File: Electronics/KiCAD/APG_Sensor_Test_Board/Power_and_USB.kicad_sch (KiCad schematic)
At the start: 10 parts, among them J4 USB_C_Receptacle_USB2.0_16P, U6 TLV1117-33

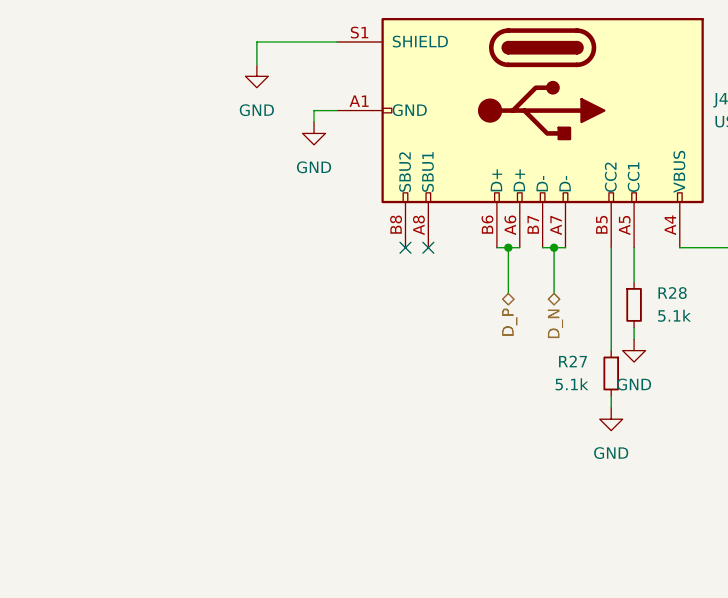
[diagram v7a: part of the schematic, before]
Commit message: TVS protection began layout
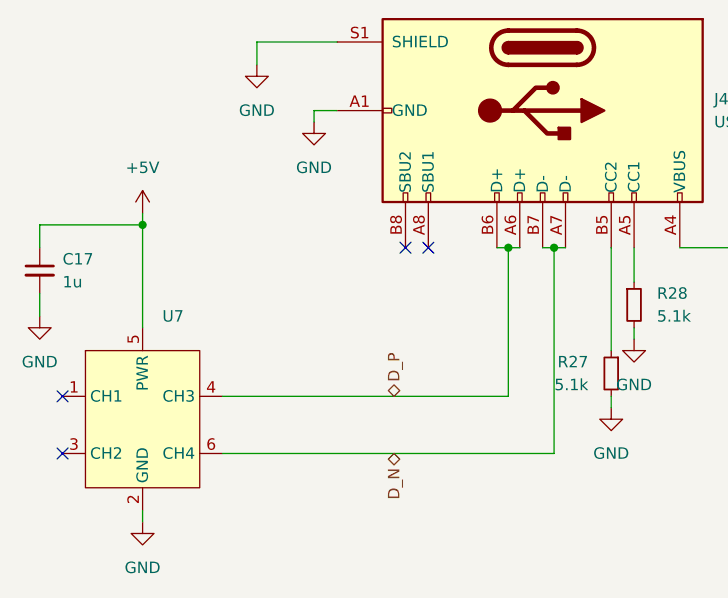
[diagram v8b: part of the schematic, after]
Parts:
- added C17: 1u, Capacitor_SMD:C_0805_2012Metric, symbol Device:C_Small
- added U7: ~, symbol Project:CM1293A-04SO
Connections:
- net +5V: now also C17.1, U7.5 (PWR)
- net D_N: now also U7.6 (CH4)
- net D_P: now also U7.4 (CH3)
- net GND: now also C17.2, U7.2 (GND)
- no-connect marks 2 -> 4
